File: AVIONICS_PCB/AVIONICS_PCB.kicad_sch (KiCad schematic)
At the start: 8 parts, among them J1 XT30PW-M, U1 ESP32-S3-DevKitC

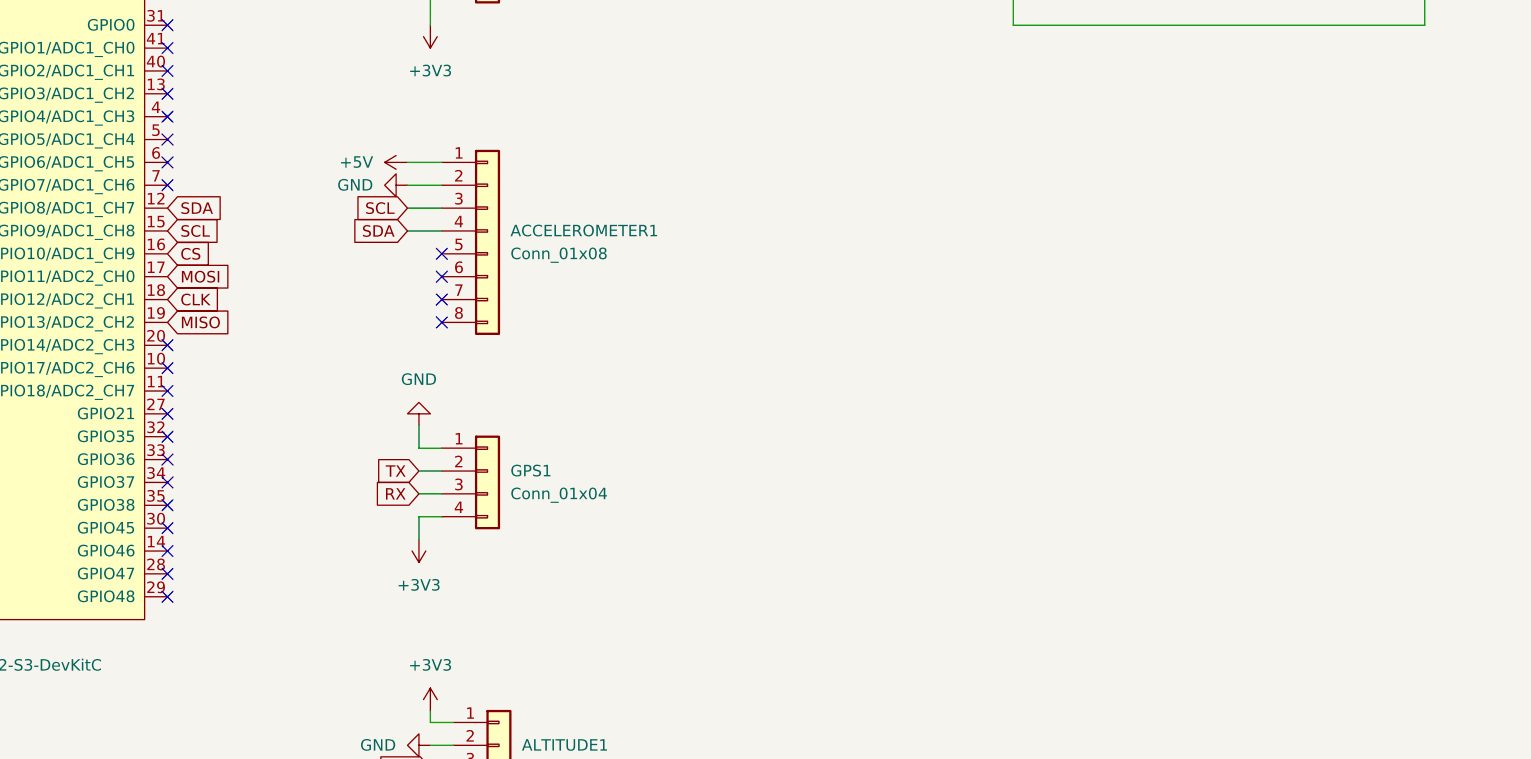
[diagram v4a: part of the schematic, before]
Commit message: Compact the board
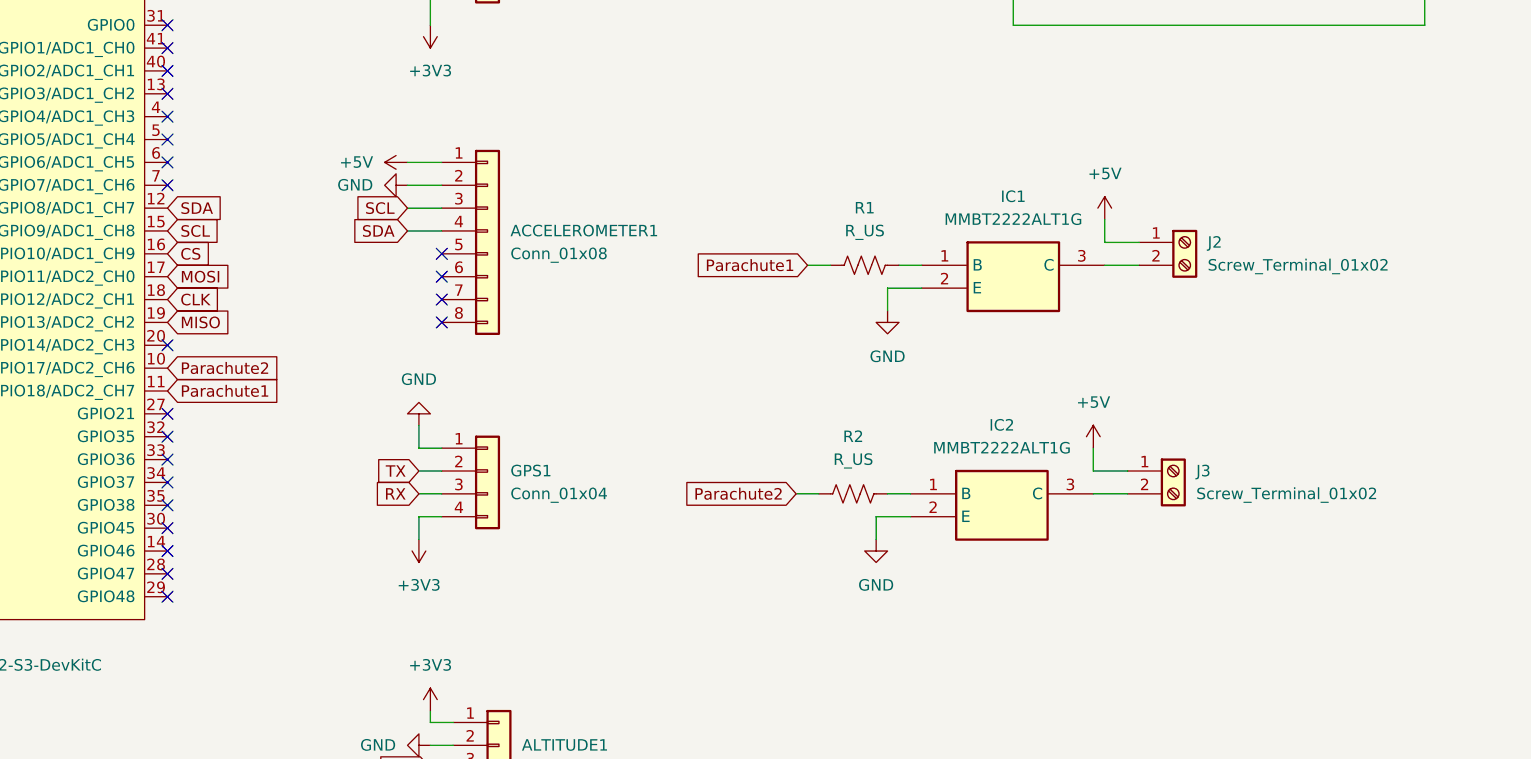
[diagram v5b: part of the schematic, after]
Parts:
- added IC1, IC2: MMBT2222ALT1G, SOT96P237X111-3N, symbol SamacSys_Parts:MMBT2222ALT1G
- added J2, J3: Screw_Terminal_01x02, TerminalBlock_Phoenix:TerminalBlock_Phoenix_MPT-0,5-2-2.54_1x02_P2.54mm_Horizontal, symbol Connector:Screw_Terminal_01x02
- added R1, R2: R_US, Resistor_SMD:R_1206_3216Metric_Pad1.30x1.75mm_HandSolder, symbol Device:R_US
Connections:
- net +5V: now also J2.1 (Pin_1), J3.1 (Pin_1)
- net GND: now also IC1.2 (E), IC2.2 (E)
- net Parachute2: now reaches U1.10 (GPIO17/ADC2_CH6)
- net Parachute2: now also R2.1
- net Parachute1: now reaches U1.11 (GPIO18/ADC2_CH7)
- net Parachute1: now also R1.1
- new net: IC1.3 (C), J2.2 (Pin_2)
- new net: IC2.1 (B), R2.2
- new net: IC1.1 (B), R1.2
- new net: IC2.3 (C), J3.2 (Pin_2)
- no-connect marks 33 -> 31

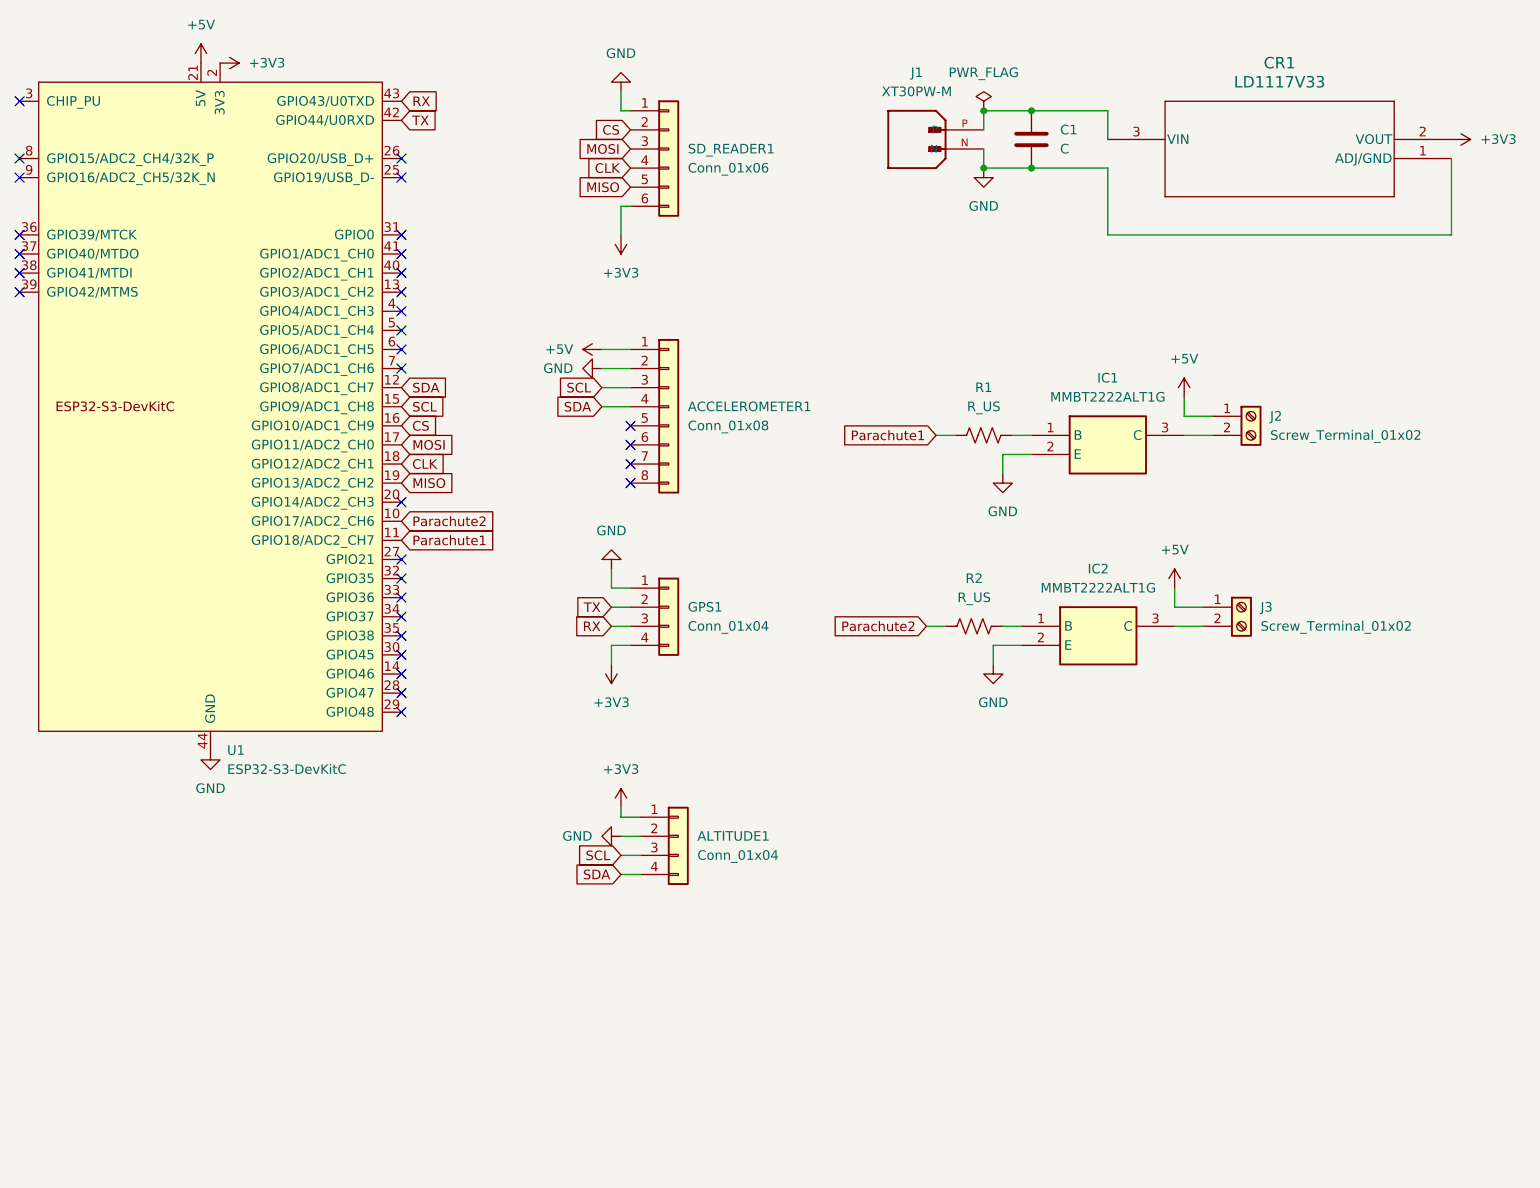
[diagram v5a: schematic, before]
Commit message: Servos
Updated the schematic to include circuitry for the servos
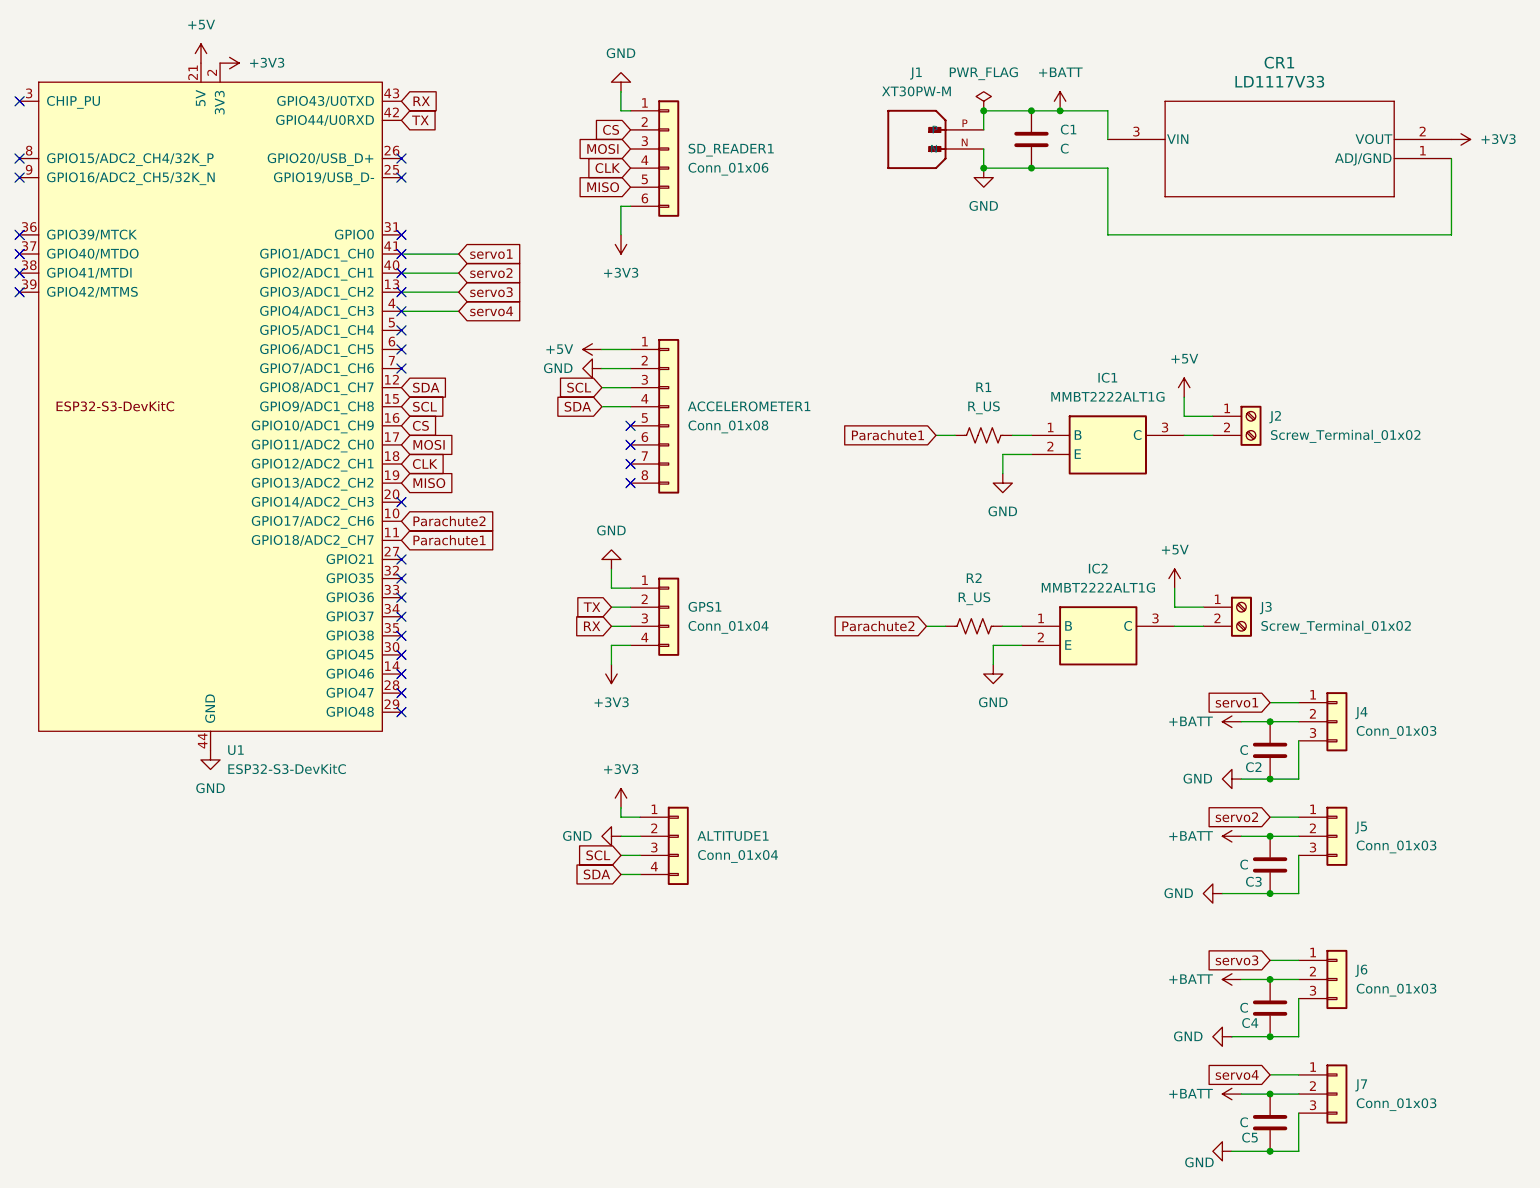
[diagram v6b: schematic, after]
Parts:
- added C2, C3, C4, C5: C, Capacitor_SMD:C_0805_2012Metric_Pad1.18x1.45mm_HandSolder, symbol Device:C
- added J4, J5, J6, J7: Conn_01x03, Connector_Molex:Molex_KK-254_AE-6410-03A_1x03_P2.54mm_Vertical, symbol Connector_Generic:Conn_01x03
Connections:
- net GND: now also C2.2, C3.2, C4.2, C5.2, J4.3 (Pin_3), J5.3 (Pin_3), J6.3 (Pin_3), J7.3 (Pin_3)
- net +BATT: now reaches C1.1, CR1.3 (VIN), J1.P
- net +BATT: now also C2.1, C3.1, C4.1, C5.1, J4.2 (Pin_2), J5.2 (Pin_2), J6.2 (Pin_2), J7.2 (Pin_2)
- net servo3: now reaches U1.13 (GPIO3/ADC1_CH2)
- net servo3: now also J6.1 (Pin_1)
- net servo4: now reaches U1.4 (GPIO4/ADC1_CH3)
- net servo4: now also J7.1 (Pin_1)
- net servo2: now reaches U1.40 (GPIO2/ADC1_CH1)
- net servo2: now also J5.1 (Pin_1)
- net servo1: now reaches U1.41 (GPIO1/ADC1_CH0)
- net servo1: now also J4.1 (Pin_1)

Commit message: NPN Transistor
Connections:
- net +5V: no longer J2.1 (Pin_1), J3.1 (Pin_1)
- net +BATT: now also J2.1 (Pin_1), J3.1 (Pin_1)
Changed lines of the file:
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@@
 	)
 	(symbol
+		(lib_id "power:+BATT")
+		(at 181.61 62.23 0)
+		(unit 1)
+		(exclude_from_sim no)
+		(in_bom yes)
+		(on_board yes)
+		(dnp no)
+		(fields_autoplaced yes)
+		(property "Reference" "#PWR027"
+			(at 181.61 66.04 0)
+			(effects
+				(font
+					(size 1.27 1.27)
+				)
+				(hide yes)
+			)
+		)
+		(property "Value" "+BATT"
+			(at 181.61 57.15 0)
+			(effects
+				(font
+					(size 1.27 1.27)
+				)
+			)
+		)
+		(property "Footprint" ""
+			(at 181.61 62.23 0)
+			(effects
+				(font
+					(size 1.27 1.27)
+				)
+				(hide yes)
+			)
+		)
+		(property "Datasheet" ""
+			(at 181.61 62.23 0)
+			(effects
+				(font
+					(size 1.27 1.27)
+				)
+				(hide yes)
+			)
+		)
+		(property "Description" "Power symbol creates a global label with name \"+BATT\""
+			(at 181.61 62.23 0)
+			(effects
+				(font
+					(size 1.27 1.27)
+				)
+				(hide yes)
+			)
+		)
+		(pin "1"
+		)
+		(instances
+			(project "AVIONICS_PCB"
+				(path "/62770ac1-9b47-4d00-b615-ae949e917d5b"
+					(reference "#PWR027")
+					(unit 1)
+				)
+			)
+		)
+	)
+	(symbol
 		(lib_id "Connector_Generic:Conn_01x04")
 		(at 113.03 90.17 0)
@@
 	)
 	(symbol
+		(lib_id "power:+BATT")
+		(at 180.34 87.63 0)
+		(unit 1)
+		(exclude_from_sim no)
+		(in_bom yes)
+		(on_board yes)
+		(dnp no)
+		(fields_autoplaced yes)
+		(property "Reference" "#PWR028"
+			(at 180.34 91.44 0)
+			(effects
+				(font
+					(size 1.27 1.27)
+				)
+				(hide yes)
+			)
+		)
+		(property "Value" "+BATT"
+			(at 180.34 82.55 0)
+			(effects
+				(font
+					(size 1.27 1.27)
+				)
+			)
+		)
+		(property "Footprint" ""
+			(at 180.34 87.63 0)
+			(effects
+				(font
+					(size 1.27 1.27)
+				)
+				(hide yes)
+			)
+		)
+		(property "Datasheet" ""
+			(at 180.34 87.63 0)
+			(effects
+				(font
+					(size 1.27 1.27)
+				)
+				(hide yes)
+			)
+		)
+		(property "Description" "Power symbol creates a global label with name \"+BATT\""
+			(at 180.34 87.63 0)
+			(effects
+				(font
+					(size 1.27 1.27)
+				)
+				(hide yes)
+			)
+		)
+		(pin "1"
+		)
+		(instances
+			(project "AVIONICS_PCB"
+				(path "/62770ac1-9b47-4d00-b615-ae949e917d5b"
+					(reference "#PWR028")
+					(unit 1)
+				)
+			)
+		)
+	)
+	(symbol
 		(lib_id "power:+3V3")
 		(at 106.68 40.64 180)
@@
 	)
 	(symbol
-		(lib_id "power:+5V")
-		(at 180.34 87.63 0)
-		(unit 1)
-		(exclude_from_sim no)
-		(in_bom yes)
-		(on_board yes)
-		(dnp no)
-		(fields_autoplaced yes)
-		(property "Reference" "#PWR017"
-			(at 180.34 91.44 0)
-			(effects
-				(font
-					(size 1.27 1.27)
-				)
-				(hide yes)
-			)
-		)
-		(property "Value" "+5V"
-			(at 180.34 82.55 0)
-			(effects
-				(font
-					(size 1.27 1.27)
-				)
-			)
-		)
-		(property "Footprint" ""
-			(at 180.34 87.63 0)
-			(effects
-				(font
-					(size 1.27 1.27)
-				)
-				(hide yes)
-			)
-		)
-		(property "Datasheet" ""
-			(at 180.34 87.63 0)
-			(effects
-				(font
-					(size 1.27 1.27)
-				)
-				(hide yes)
-			)
-		)
-		(property "Description" "Power symbol creates a global label with name \"+5V\""
-			(at 180.34 87.63 0)
-			(effects
-				(font
-					(size 1.27 1.27)
-				)
-				(hide yes)
-			)
-		)
-		(pin "1"
-		)
-		(instances
-			(project "AVIONICS_PCB"
-				(path "/62770ac1-9b47-4d00-b615-ae949e917d5b"
-					(reference "#PWR017")
-					(unit 1)
-				)
-			)
-		)
-	)
-	(symbol
 		(lib_id "power:+BATT")
 		(at 189.23 105.41 90)
@@
 					(unit 1)
 				)
-			)
-		)
-	)
-	(symbol
-		(lib_id "power:+5V")
-		(at 181.61 62.23 0)
-		(unit 1)
-		(exclude_from_sim no)
-		(in_bom yes)
-		(on_board yes)
-		(dnp no)
-		(fields_autoplaced yes)
-		(property "Reference" "#PWR015"
-			(at 181.61 66.04 0)
-			(effects
-				(font
-					(size 1.27 1.27)
-				)
-				(hide yes)
-			)
-		)
-		(property "Value" "+5V"
-			(at 181.61 57.15 0)
-			(effects
-				(font
-					(size 1.27 1.27)
-				)
-			)
-		)
-		(property "Footprint" ""
-			(at 181.61 62.23 0)
-			(effects
-				(font
-					(size 1.27 1.27)
-				)
-				(hide yes)
-			)
-		)
-		(property "Datasheet" ""
-			(at 181.61 62.23 0)
-			(effects
-				(font
-					(size 1.27 1.27)
-				)
-				(hide yes)
-			)
-		)
-		(property "Description" "Power symbol creates a global label with name \"+5V\""
-			(at 181.61 62.23 0)
-			(effects
-				(font
-					(size 1.27 1.27)
-				)
-				(hide yes)
-			)
-		)
-		(pin "1"
-		)
-		(instances
-			(project ""
-				(path "/62770ac1-9b47-4d00-b615-ae949e917d5b"
-					(reference "#PWR015")
-					(unit 1)
-				)

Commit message: Board v2
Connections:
- net +3V3: now also C2.1, C3.1, C4.1, C5.1, J2.1 (Pin_1), J3.1 (Pin_1), J4.2 (Pin_2), J5.2 (Pin_2), J6.2 (Pin_2), J7.2 (Pin_2)
- net servo1: now also U1.35 (GPIO38); no longer U1.41 (GPIO1/ADC1_CH0)
- net servo2: now also U1.34 (GPIO37); no longer U1.40 (GPIO2/ADC1_CH1)
- net servo3: now also U1.33 (GPIO36); no longer U1.13 (GPIO3/ADC1_CH2)
- net servo4: now also U1.32 (GPIO35); no longer U1.4 (GPIO4/ADC1_CH3)
- removed net +BATT: C1.1, C2.1, C3.1, C4.1, C5.1, CR1.3 (VIN), J1.P, J2.1 (Pin_1), J3.1 (Pin_1), J4.2 (Pin_2), J5.2 (Pin_2), J6.2 (Pin_2), J7.2 (Pin_2)
- new net: C1.1, CR1.3 (VIN), J1.P
- no-connect marks 31 -> 27
